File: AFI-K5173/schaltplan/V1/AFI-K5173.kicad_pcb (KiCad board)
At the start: 2 copper layers, 100 x 160 mm, 44 parts, among them J1 KES BUS, J2 IDE Chan A, J3 Front Panel, U1 74HCT573, U10 74HCT04, U11 74HCT04, U12 74HCT04, U13 74AHCT04, U14 74HCT32, U15 74HCT138, U16 74HCT08, U17 74HCT20, U18 74HCT20, U19 74HCT74, U2 74HCT573, U20 74HCT138, U3 74HCT573, U4 74HCT573, U5 74HCT573, U6 74HCT573, U7 74HCT640, U8 74HCT573, U9 SST39SF040

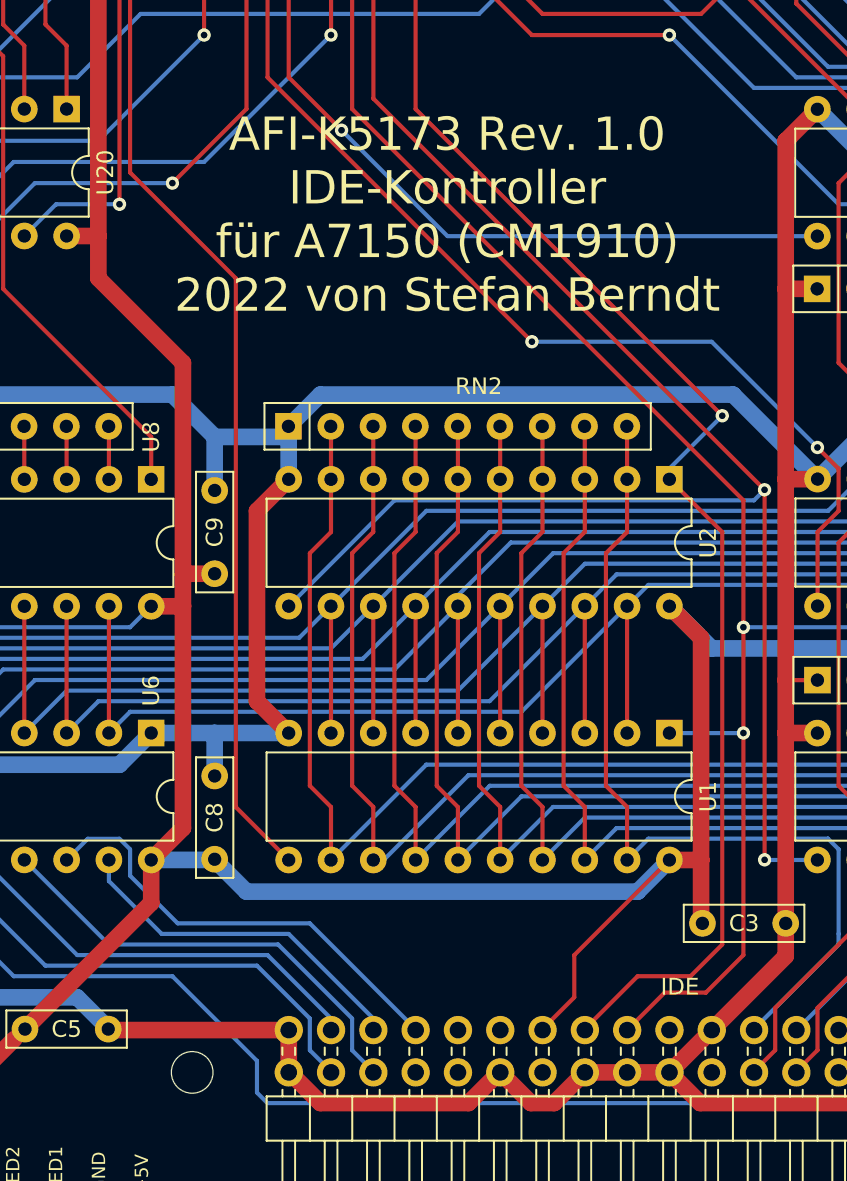
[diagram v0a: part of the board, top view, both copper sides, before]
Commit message: Bigfix Schaltung/PCB: Pin 39 des IDE-Steckers darf nicht auf Masse liegen. Das verursacht eine exrem lange Bootphase bei bestimmten Platten-Konfigurationen.
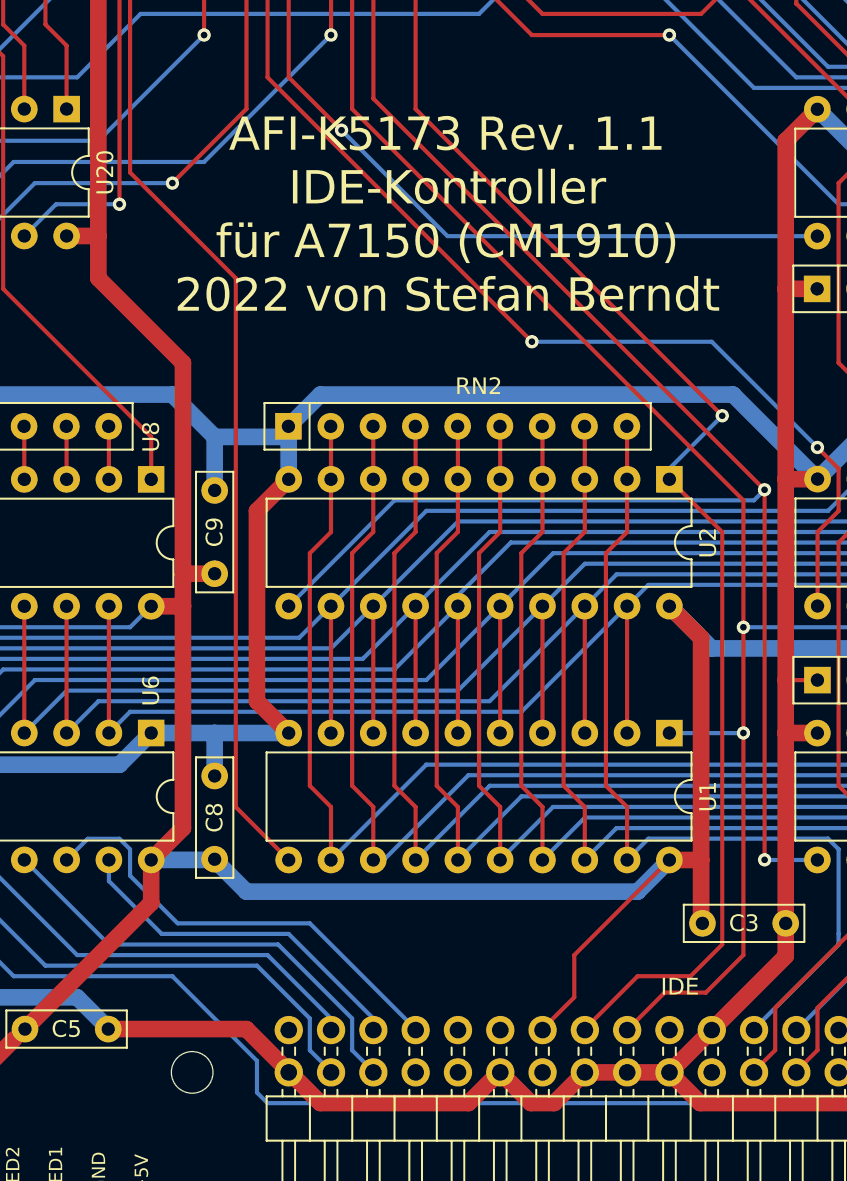
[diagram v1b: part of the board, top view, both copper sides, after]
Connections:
- J2 pad 39: GND -> unconnected-(J2-Pad39)
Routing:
- net GND: track 1040.5 -> 1039.1 mm
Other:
- board text added: "AFI-K5173 Rev. 1.1 IDE-Kontroller für A7150 (CM1910) 2022 von Stefan Berndt"
- board text removed: "AFI-K5173 Rev. 1.0 IDE-Kontroller für A7150 (CM1910) 2022 von Stefan Berndt"

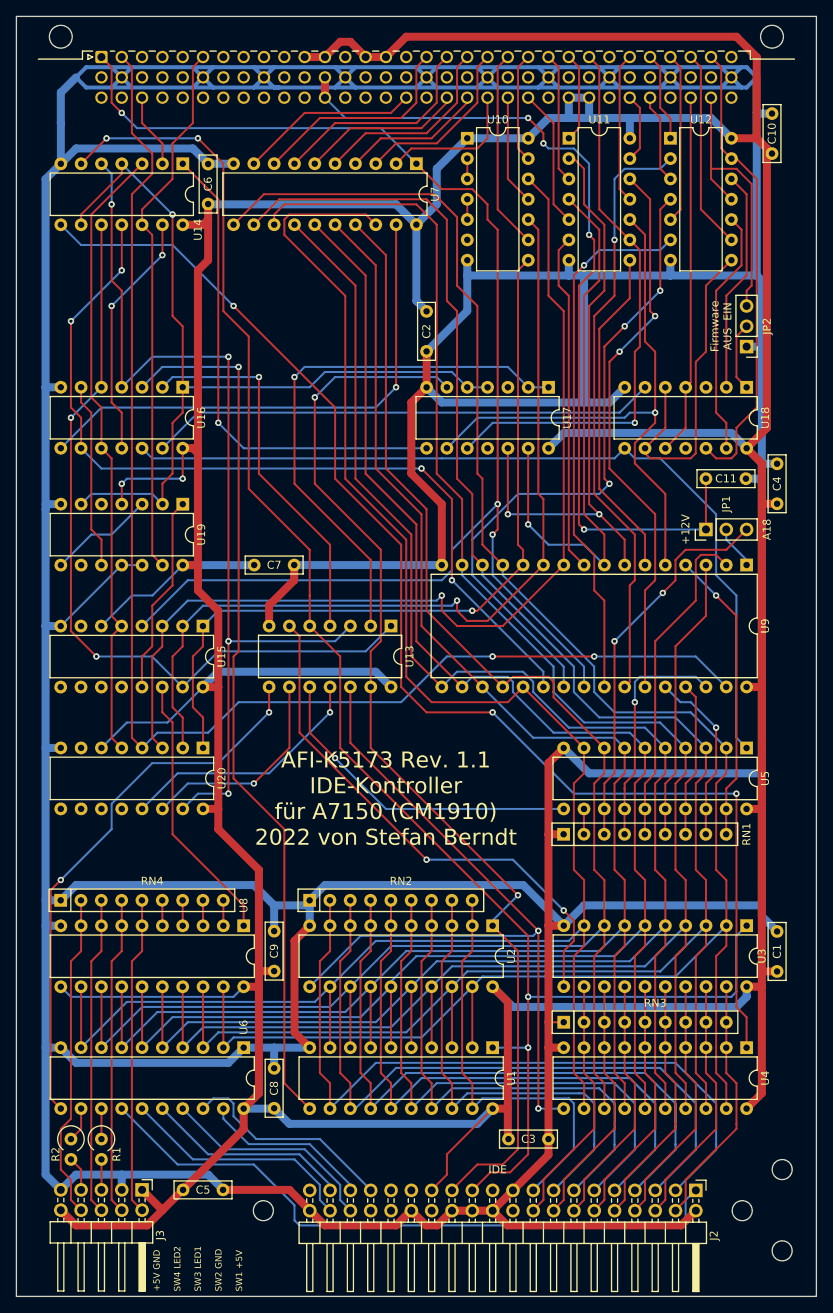
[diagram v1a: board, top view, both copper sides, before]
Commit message: Schaltung/PCB: Anschluss für USB-Kontroller-Platine hinzugefügt
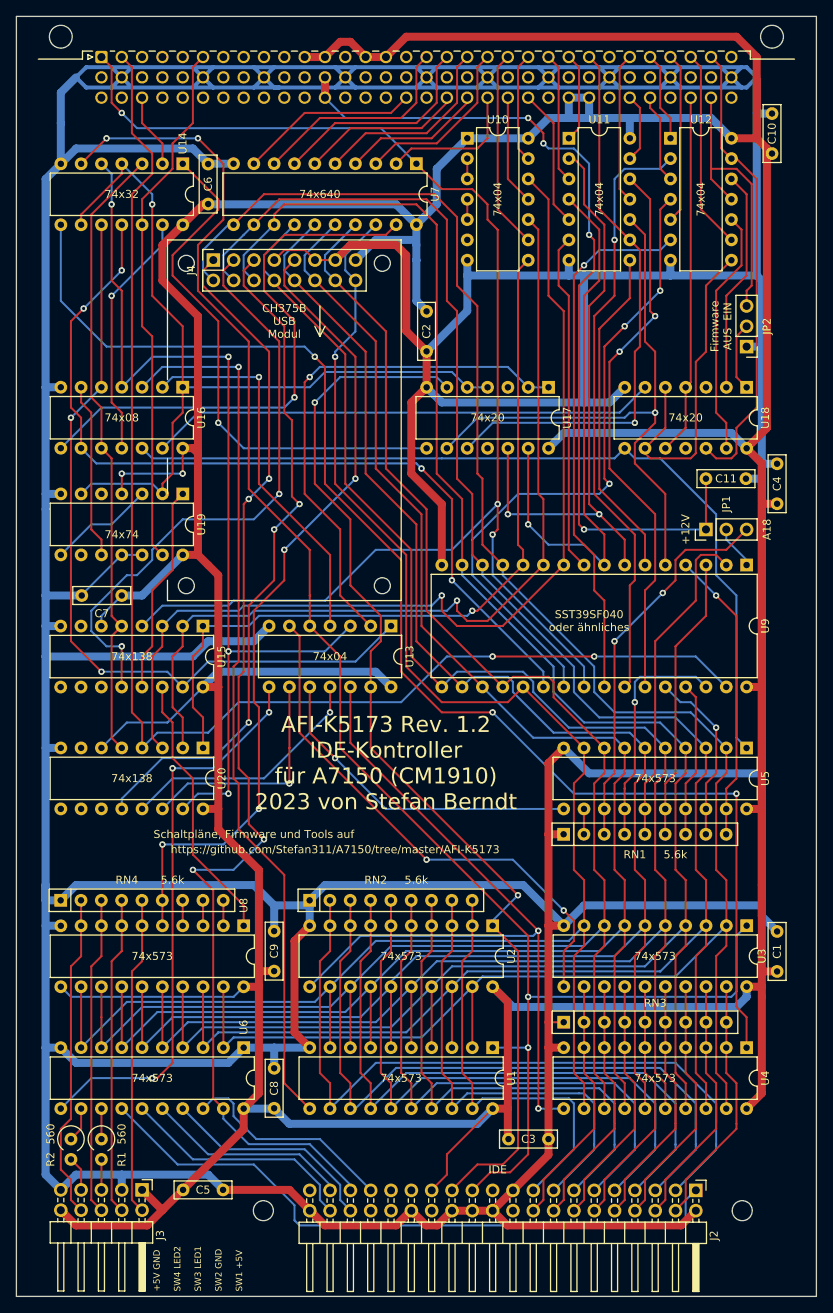
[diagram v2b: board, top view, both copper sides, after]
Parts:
- removed the ? at (139.7, 205.7)
- removed the ? at (139.7, 195.6)
- added ?: , , F.Cu at (64.8, 81.9)
- added ?: , , F.Cu at (89.5, 121.9)
- added ?: , , F.Cu at (77.5, 88.9)
- added ?: , , F.Cu at (82.8, 91.0)
- added J4: Conn_01x16_Female, Connector_PinSocket_2.54mm:PinSocket_2x08_P2.54mm_Vertical, F.Cu at (68.6, 81.9)
- moved C7 17.0 mm to (57.1, 123.8), turned to 180 degrees
- moved U19 1.28 mm to (64.8, 111.1)
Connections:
- U15 pad 12: unconnected-(U15-Pad12) -> /URD
- U20 pad 12: unconnected-(U20-Pad12) -> /UWR
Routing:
- net /HA0: track 21.3 -> 142.4 mm, vias 0 -> 4
- net Net-(J4-Pad9): track 2.55 -> 101.8 mm, vias 0 -> 4
- net /UWR: track 0.00 -> 85.6 mm, vias 0 -> 3
- net /URD: track 0.00 -> 75.2 mm, vias 0 -> 2
- net GND: track 1039.1 -> 1076.8 mm
- net /ID7: track 234.8 -> 221.7 mm, vias 0 -> 1
- net /ID0: track 248.2 -> 257.7 mm
- net /ID2: track 238.6 -> 247.7 mm
- net /ID1: track 243.1 -> 252.2 mm
- net /IRD2: track 161.8 -> 168.5 mm
- net Net-(U14-Pad1): track 61.6 -> 66.3 mm
- net Net-(U16-Pad8): track 65.4 -> 69.3 mm
- net /ID5: track 218.0 -> 221.2 mm
- net /ID6: track 215.1 -> 218.2 mm
- net /ID4: track 225.2 -> 228.4 mm
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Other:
- board text added: "5.6k"
- board text added: "560"
- board text added: "74x04"
- board text added: "74x08"
- board text added: "74x138"
- board text added: "74x20"
- board text added: "74x32"
- board text added: "74x573"
- board text added: "74x640"
- board text added: "74x74"
- board text added: "AFI-K5173 Rev. 1.2 IDE-Kontroller für A7150 (CM1910) 2023 von Stefan Berndt"
- board text added: "CH375B USB Modul"
- board text added: "SST39SF040 oder ähnliches"
- board text added: "Schaltpläne, Firmware und Tools auf"
- board text added: "https://github.com/Stefan311/A7150/tree/master/AFI-K5173"
- board text removed: "AFI-K5173 Rev. 1.1 IDE-Kontroller für A7150 (CM1910) 2022 von Stefan Berndt"

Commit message: Schaltungsänderung und Layout V0.3
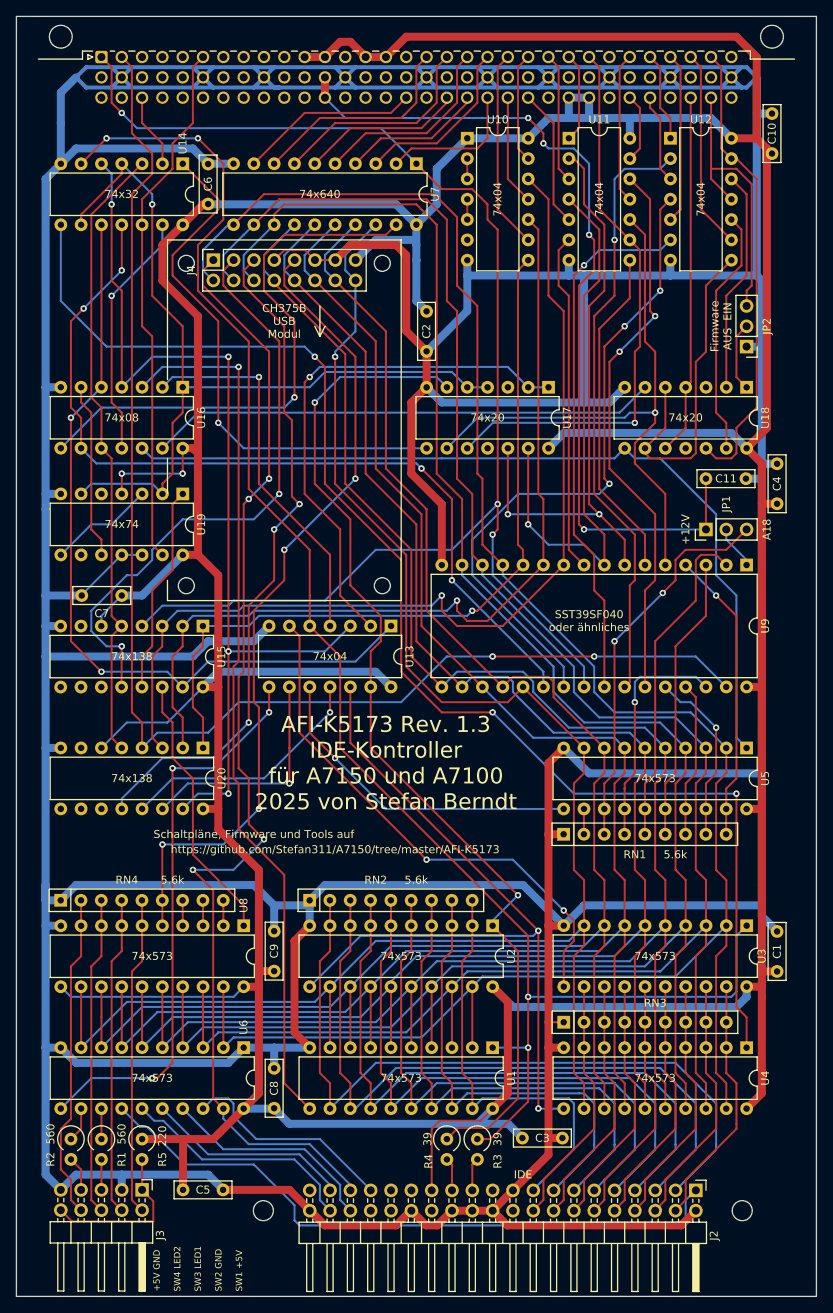
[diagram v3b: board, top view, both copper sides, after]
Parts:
- added R3: 39, Resistor_THT:R_Axial_DIN0309_L9.0mm_D3.2mm_P2.54mm_Vertical, F.Cu at (101.6, 191.8)
- added R4: 39, Resistor_THT:R_Axial_DIN0309_L9.0mm_D3.2mm_P2.54mm_Vertical, F.Cu at (97.8, 191.8)
- added R5: 220, Resistor_THT:R_Axial_DIN0309_L9.0mm_D3.2mm_P2.54mm_Vertical, F.Cu at (59.7, 191.8)
- moved C3 1.74 mm to (107.2, 191.6)
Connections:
- J2 pad 23: /HWR -> Net-(J2-Pin_23)
- J2 pad 25: /HRD -> Net-(J2-Pin_25)
- J3 pad 1: +5V -> Net-(J3-Pin_1)
- J3 pad 10: +5V -> Net-(J3-Pin_1)
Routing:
- net Net-(J3-Pin_1): track 0.00 -> 20.5 mm
- net +5V: track 701.6 -> 692.7 mm
- net /HWR: track 211.0 -> 203.9 mm
- net /HRD: track 136.3 -> 130.6 mm
- net Net-(J2-Pin_25): track 0.00 -> 4.14 mm
- net Net-(J2-Pin_23): track 0.00 -> 4.13 mm
- net GND: track 1076.8 -> 1078.6 mm
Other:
- board text added: "220"
- board text added: "39"
- board text added: "AFI-K5173 Rev. 1.3 IDE-Kontroller für A7150 und A7100 2025 von Stefan Berndt"
- board text removed: "AFI-K5173 Rev. 1.2 IDE-Kontroller für A7150 (CM1910) 2023 von Stefan Berndt"
